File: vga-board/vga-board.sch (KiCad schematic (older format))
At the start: 48 parts, among them J1 EXP, J2 EXP, J3 Conn_02x05_Odd_Even, J4 DB15_Female_HighDensity, U1 XC95144XL-TQ100, U2 IS61C5128AL-10TLI, X1 ABLNO

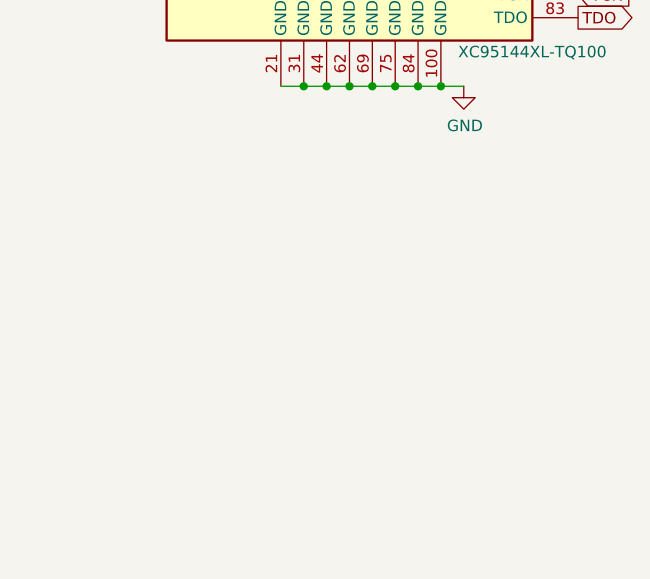
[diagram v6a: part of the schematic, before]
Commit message: reroute main board and IO board again
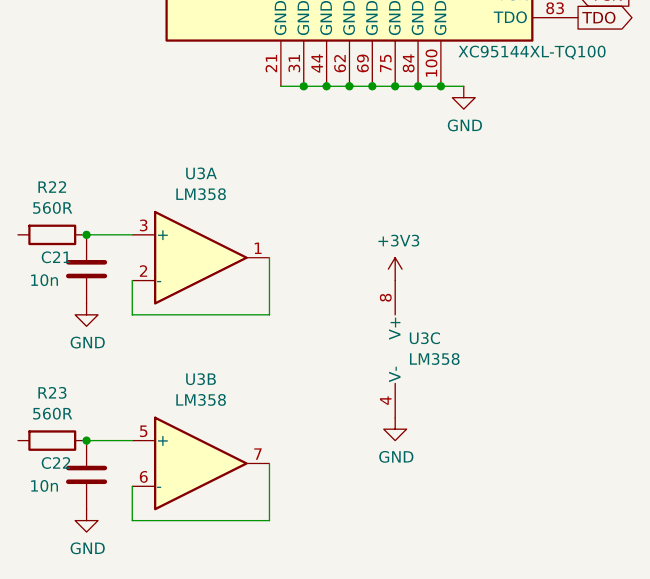
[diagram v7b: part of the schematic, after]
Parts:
- added C21, C22: 10n, Capacitor_SMD:C_0402_1005Metric, symbol Device:C
- added R22, R23: 560R, Resistor_SMD:R_0402_1005Metric, symbol Device:R
- added U3: LM358, symbol Amplifier_Operational:LM358
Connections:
- net +3V3: now also U3.8 (V+)
- net GND: now also C21.2, C22.2, U3.4 (V-)
- new net: U3.1, U3.2 (-)
- new net: C21.1, R22.1, U3.3 (+)
- new net: C22.1, R23.1, U3.5 (+)
- new net: U3.6 (-), U3.7
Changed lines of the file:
@@
 Text GLabel 1150 4850 0    50   Output ~ 0
 VSYNC
+$Comp
+L Amplifier_Operational:LM358 U3
+U 1 1 6003253D
+P 1500 7000
+F 0 "U3" H 1500 7367 50  0000 C CNN
+F 1 "LM358" H 1500 7276 50  0000 C CNN
+F 2 "" H 1500 7000 50  0001 C CNN
+F 3 "http://www.ti.com/lit/ds/symlink/lm2904-n.pdf" H 1500 7000 50  0001 C CNN
+	1    1500 7000
+	1    0    0    -1
+$EndComp
+$Comp
+L Amplifier_Operational:LM358 U3
+U 3 1 60034E12
+P 2450 7400
+F 0 "U3" H 2408 7446 50  0000 L CNN
+F 1 "LM358" H 2408 7355 50  0000 L CNN
+F 2 "" H 2450 7400 50  0001 C CNN
+F 3 "http://www.ti.com/lit/ds/symlink/lm2904-n.pdf" H 2450 7400 50  0001 C CNN
+	3    2450 7400
+	1    0    0    -1
+$EndComp
+$Comp
+L Device:R R22
+U 1 1 600621D5
+P 850 6900
+F 0 "R22" V 643 6900 50  0000 C CNN
+F 1 "560R" V 734 6900 50  0000 C CNN
+F 2 "Resistor_SMD:R_0402_1005Metric" V 780 6900 50  0001 C CNN
+F 3 "~" H 850 6900 50  0001 C CNN
+	1    850  6900
+	0    1    1    0
+$EndComp
+$Comp
+L Device:C C21
+U 1 1 60067DB1
+P 1000 7050
+F 0 "C21" H 800 7100 50  0000 L CNN
+F 1 "10n" H 750 7000 50  0000 L CNN
+F 2 "Capacitor_SMD:C_0402_1005Metric" H 1038 6900 50  0001 C CNN
+F 3 "~" H 1000 7050 50  0001 C CNN
+	1    1000 7050
+	1    0    0    -1
+$EndComp
+Wire Wire Line
+	1000 6900 1200 6900
+Connection ~ 1000 6900
+$Comp
+L power:GND #PWR0110
+U 1 1 6007BBD7
+P 2350 7700
+F 0 "#PWR0110" H 2350 7450 50  0001 C CNN
+F 1 "GND" H 2355 7527 50  0000 C CNN
+F 2 "" H 2350 7700 50  0001 C CNN
+F 3 "" H 2350 7700 50  0001 C CNN
+	1    2350 7700
+	1    0    0    -1
+$EndComp
+$Comp
+L power:GND #PWR0111
+U 1 1 600A58CC
+P 1000 7200
+F 0 "#PWR0111" H 1000 6950 50  0001 C CNN
+F 1 "GND" H 1005 7027 50  0000 C CNN
+F 2 "" H 1000 7200 50  0001 C CNN
+F 3 "" H 1000 7200 50  0001 C CNN
+	1    1000 7200
+	1    0    0    -1
+$EndComp
+Wire Wire Line
+	1200 7100 1200 7250
+Wire Wire Line
+	1200 7250 1800 7250
+Wire Wire Line
+	1800 7250 1800 7000
+$Comp
+L Amplifier_Operational:LM358 U3
+U 2 1 600AE726
+P 1500 7900
+F 0 "U3" H 1500 8267 50  0000 C CNN
+F 1 "LM358" H 1500 8176 50  0000 C CNN
+F 2 "" H 1500 7900 50  0001 C CNN
+F 3 "http://www.ti.com/lit/ds/symlink/lm2904-n.pdf" H 1500 7900 50  0001 C CNN
+	2    1500 7900
+	1    0    0    -1
+$EndComp
+$Comp
+L Device:R R23
+U 1 1 600B4C08
+P 850 7800
+F 0 "R23" V 643 7800 50  0000 C CNN
+F 1 "560R" V 734 7800 50  0000 C CNN
+F 2 "Resistor_SMD:R_0402_1005Metric" V 780 7800 50  0001 C CNN
+F 3 "~" H 850 7800 50  0001 C CNN
+	1    850  7800
+	0    1    1    0
+$EndComp
+$Comp
+L Device:C C22
+U 1 1 600B50D0
+P 1000 7950
+F 0 "C22" H 800 8000 50  0000 L CNN
+F 1 "10n" H 750 7900 50  0000 L CNN
+F 2 "Capacitor_SMD:C_0402_1005Metric" H 1038 7800 50  0001 C CNN
+F 3 "~" H 1000 7950 50  0001 C CNN
+	1    1000 7950
+	1    0    0    -1
+$EndComp
+Wire Wire Line
+	1000 7800 1200 7800
+Connection ~ 1000 7800
+$Comp
+L power:GND #PWR0112
+U 1 1 600B50DC
+P 1000 8100
+F 0 "#PWR0112" H 1000 7850 50  0001 C CNN
+F 1 "GND" H 1005 7927 50  0000 C CNN
+F 2 "" H 1000 8100 50  0001 C CNN
+F 3 "" H 1000 8100 50  0001 C CNN
+	1    1000 8100
+	1    0    0    -1
+$EndComp
+Wire Wire Line
+	1200 8000 1200 8150
+Wire Wire Line
+	1200 8150 1800 8150
+Wire Wire Line
+	1800 8150 1800 7900
+$Comp
+L power:+3V3 #PWR0113
+U 1 1 600E6C1F
+P 2350 7100
+F 0 "#PWR0113" H 2350 6950 50  0001 C CNN
+F 1 "+3V3" H 2365 7273 50  0000 C CNN
+F 2 "" H 2350 7100 50  0001 C CNN
+F 3 "" H 2350 7100 50  0001 C CNN
+	1    2350 7100
+	1    0    0    -1
+$EndComp
 $EndSCHEMATC
